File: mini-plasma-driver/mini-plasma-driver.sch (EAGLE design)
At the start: 93 parts, among them IC1 IR21844D, IC2 74LS19N, IC3 NE555N, IC5 IR21844D, J1 12v IN, Q1 STH60N10W, Q3 2N2369, Q4 2N2369, Q7 STH60N10W, Q8 STH60N10W, Q9 STH60N10W

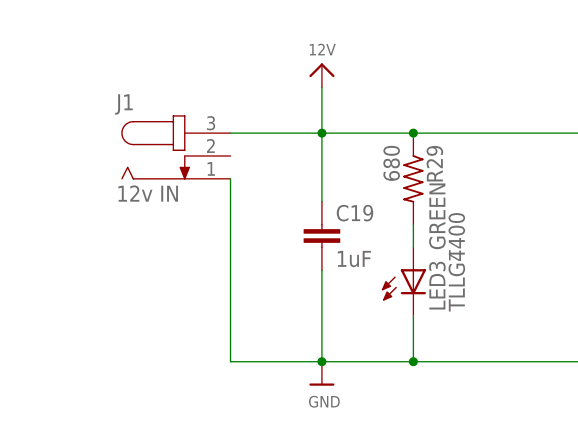
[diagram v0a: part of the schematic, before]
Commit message: replace 12v barrel connector
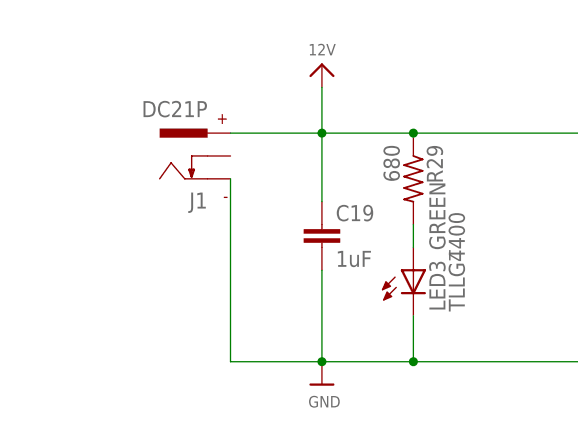
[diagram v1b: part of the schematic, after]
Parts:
- J1: value 12v IN -> DC21P; device con-jack:JACK-PLUG0 -> keves:DC21P
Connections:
- net 12V: now also J1.+; no longer J1.3
- net GND: now also J1.-; no longer J1.1
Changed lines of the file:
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@@
 <part name="TP2" library="microbuilder" deviceset="TESTPOINT" device="0.1&quot;"/>
 <part name="R28" library="rcl" library_urn="urn:adsk.eagle:library:334" deviceset="R-TRIMM" device="3296Y" package3d_urn="urn:adsk.eagle:package:23741/1" value="50K Bourns PV37"/>
-<part name="J1" library="con-jack" library_urn="urn:adsk.eagle:library:154" deviceset="JACK-PLUG" device="0" package3d_urn="urn:adsk.eagle:package:7492/1" value="12v IN"/>
 <part name="12V2" library="microbuilder" deviceset="12V" device=""/>
 <part name="R29" library="rcl" library_urn="urn:adsk.eagle:library:334" deviceset="R-US_" device="0207/10" package3d_urn="urn:adsk.eagle:package:23491/1" value="680"/>
@@
 <part name="TP10" library="microbuilder" deviceset="TESTPOINT" device="0.1&quot;"/>
 <part name="TP11" library="microbuilder" deviceset="TESTPOINT" device="0.1&quot;"/>
+<part name="J1" library="keves" deviceset="DC21P" device=""/>
 </parts>
 <sheets>
@@
 <instance part="TP2" gate="G$1" x="-17.78" y="93.98" rot="R180"/>
 <instance part="R28" gate="G$1" x="-76.2" y="66.04"/>
-<instance part="J1" gate="G$1" x="-91.44" y="177.8"/>
 <instance part="12V2" gate="G$1" x="-76.2" y="187.96"/>
 <instance part="R29" gate="G$1" x="-66.04" y="175.26" rot="R270"/>
@@
 <instance part="TP10" gate="G$1" x="72.39" y="38.1" rot="R90"/>
 <instance part="TP11" gate="G$1" x="-93.98" y="-25.4" rot="R90"/>
+<instance part="J1" gate="G$1" x="-86.36" y="177.8" rot="R180"/>
 </instances>
 <busses>
@@
 <wire x1="-76.2" y1="180.34" x2="-66.04" y2="180.34" width="0.1524" layer="91"/>
 <pinref part="C19" gate="G$1" pin="1"/>
-<pinref part="J1" gate="G$1" pin="3"/>
 <pinref part="JP3" gate="G$1" pin="1"/>
 <wire x1="-38.1" y1="185.42" x2="-38.1" y2="180.34" width="0.1524" layer="91"/>
 <wire x1="-38.1" y1="180.34" x2="-66.04" y2="180.34" width="0.1524" layer="91"/>
 <junction x="-66.04" y="180.34"/>
+<pinref part="J1" gate="G$1" pin="+"/>
 </segment>
 <segment>
@@
 <junction x="-76.2" y="154.94"/>
 <pinref part="C19" gate="G$1" pin="2"/>
-<pinref part="J1" gate="G$1" pin="1"/>
 <wire x1="-86.36" y1="175.26" x2="-86.36" y2="154.94" width="0.1524" layer="91"/>
 <pinref part="JP3" gate="G$1" pin="2"/>
@@
 <pinref part="GND7" gate="G$1" pin="GND"/>
 <pinref part="LED3_GREEN" gate="G$1" pin="C"/>
+<pinref part="J1" gate="G$1" pin="-"/>
 </segment>
 </net>
